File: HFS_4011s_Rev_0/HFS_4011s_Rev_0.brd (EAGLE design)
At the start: 44.5 x 47 mm, 63 parts, among them IC1 CP2104, J1 2X06, J2 2X12, J3 1X02, J4 microUSB, J5 1X02, J6 MOLEX_IGRID_15X2CONNECTOR, Q1 mmbt2222, Q2 mmbt2222, Q3 MMUN2133LT1G, Q4 BSS138, Q5 BSS138, SW2 KMR2, U1 TPS61090RSAR, U2 MCP73831T-2ACI/OT, U3 AD5693R, U4 LM3671MF-3.3/NOPB, X2 ESP32_WROOM32_SKINNY

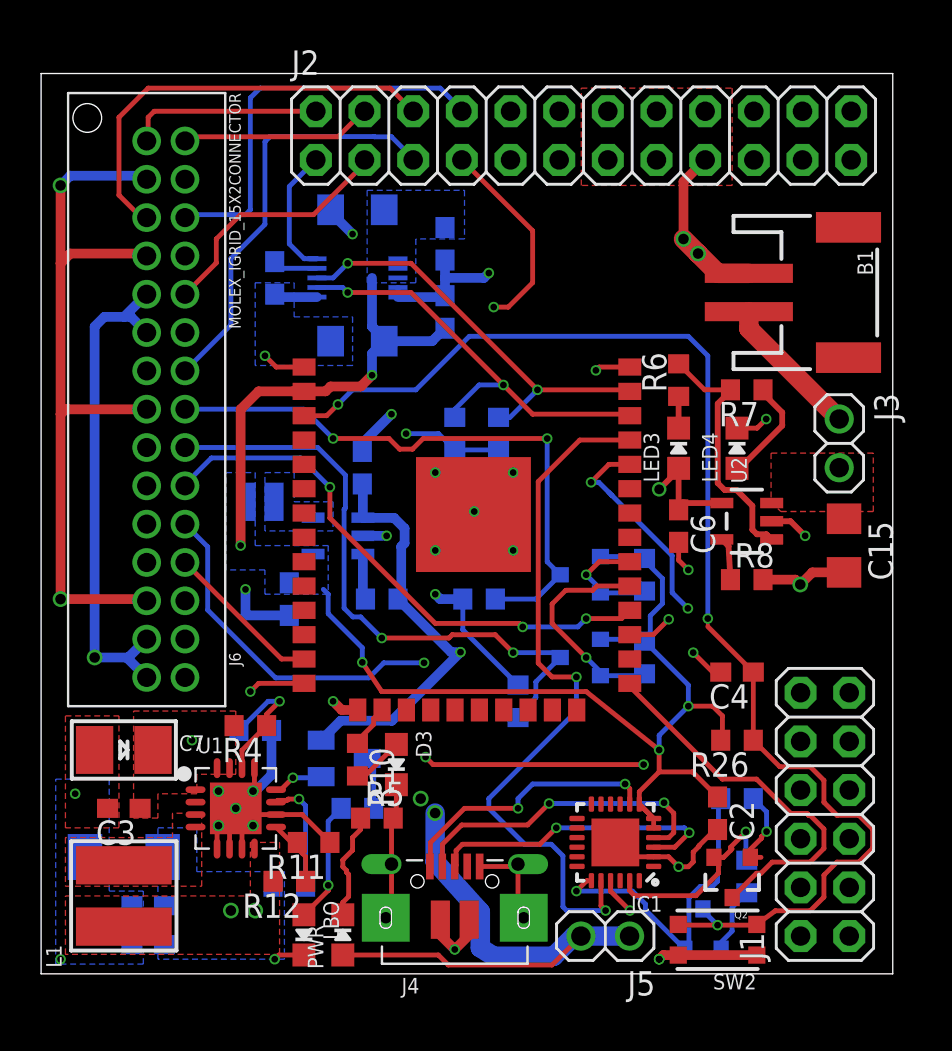
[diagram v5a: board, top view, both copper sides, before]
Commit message: Renumbered components and fixing DRC errors.
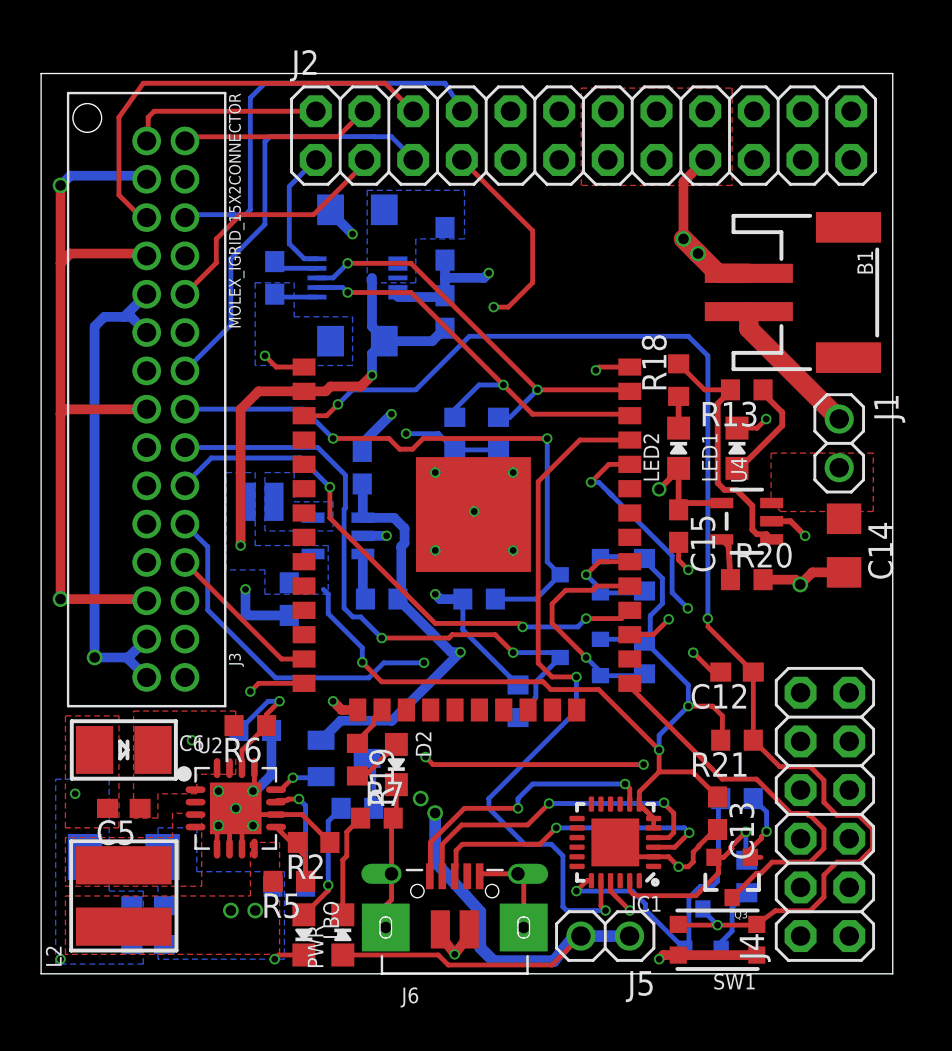
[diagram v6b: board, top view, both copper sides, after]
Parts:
- removed R23: 5.1k, rcl:R0603
- removed R24, R25, R26: 10k, rcl:R0603
- added R1: 100K, rcl:R0603
- added R13, R3: 1K, rcl:R0603
- added R15: 5.1k, rcl:R0603
- C10: value 22uF -> 10uF; device rcl:C0603 -> SparkFun-Retired:EIA3216
- C11: value 10uF -> 0.1uF
- C12: value 10nF -> 1uF
- C13: device SparkFun-Retired:EIA3216 -> rcl:C0603
- C14: value 10uF -> 4.7uF; device SparkFun-Retired:EIA3216 -> rcl:C1206
- C15: value 4.7uF -> 10µF; device rcl:C1206 -> rcl:C0603
- C2: value 10uF -> 22uF
- C3: value 2.2uF -> 10uF
- C4: value 1uF -> 0.1uF
- C5: value 0.1uF -> 2.2uF
- C6: value 10µF -> 100uF/6V; device rcl:C0603 -> microbuilder:EIA3528-21/B-R
- C7: value 100uF/6V -> 10uF; device microbuilder:EIA3528-21/B-R -> SparkFun-Retired:EIA3216
- C9: value 0.1uF -> 10nF
- J1: value 2X06 -> 1X02; device HFS4011sCustom:2X06 -> HFS4011sCustom:1X02
- J3: value 1X02 -> MOLEX_IGRID_15X2CONNECTOR; device HFS4011sCustom:1X02 -> HFS4011sCustom:MOLEX_IGRID15X2CONNECTOR
- J4: value microUSB -> 2X06; device microbuilder:4UCONN_20329 -> HFS4011sCustom:2X06
- J6: value MOLEX_IGRID_15X2CONNECTOR -> microUSB; device HFS4011sCustom:MOLEX_IGRID15X2CONNECTOR -> microbuilder:4UCONN_20329
- L1: value VLC5045-6.8uH -> 2.2uH/NRH2412T2R2MNGH; device microbuilder:INDUCTOR_5X5MM_TDK_VLC5045 -> microbuilder:INDUCTOR_TAIYOYUDEN_NRH2412T
- L2: value 2.2uH/NRH2412T2R2MNGH -> VLC5045-6.8uH; device microbuilder:INDUCTOR_TAIYOYUDEN_NRH2412T -> microbuilder:INDUCTOR_5X5MM_TDK_VLC5045
- Q1: value mmbt2222 -> MMUN2133LT1G; device SparkFun:SOT23-3 -> transistor:SC59-BEC
- Q3: value MMUN2133LT1G -> mmbt2222; device transistor:SC59-BEC -> SparkFun:SOT23-3
- R10: value 1K -> 10k
- R11: value 340K -> 5k
- R12: value 1.87Mohm -> 5k
- R14: value 100K -> 5.1k
- R17: value 5k -> 5.1k
- R18: value 5k -> 470
- R19: value 5.1k -> 1K
- R20: value 1K -> 2k
- R21: value 5.1k -> 10k
- R4: value 1.87Mohm -> 200K
- R5: value 1K -> 1.87Mohm
- R6: value 470 -> 1.87Mohm
- R8: value 2k -> 340K
- R9: value 200K -> 10k
- U1: value TPS61090RSAR -> LM3671MF-3.3/NOPB; device microbuilder:PVQFN-16 -> microbuilder:SOT23-5
- U2: value MCP73831T-2ACI/OT -> TPS61090RSAR; device microbuilder:SOT23-5 -> microbuilder:PVQFN-16
- U4: value LM3671MF-3.3/NOPB -> MCP73831T-2ACI/OT
- moved J3 35.4 mm to (6.35, 30.5)
- moved C4 33.9 mm to (5.59, 1.52), flipped to the bottom, turned to 0 degrees
- moved C12 31.7 mm to (36.3, 15.7), flipped to the top, turned to 180 degrees
- moved C6 31.2 mm to (4.32, 11.7), turned to 0 degrees
- moved C13 31.0 mm to (35.3, 8.38), flipped to the top, turned to 270 degrees
- moved C14 30.9 mm to (41.9, 22.4), flipped to the top, turned to 270 degrees
- moved C7 30.7 mm to (16.5, 39.9), flipped to the bottom, turned to 180 degrees
- moved U2 30.6 mm to (10.2, 8.64), turned to 0 degrees
- moved J6 30.3 mm to (21.6, 4.32), turned to 0 degrees
- moved R7 29.5 mm to (17.5, 8.13), turned to 0 degrees
- moved R8 28.7 mm to (13.0, 4.57), flipped to the bottom, turned to 180 degrees
- moved R6 28.7 mm to (10.9, 13.0), turned to 180 degrees
- moved R9 26.8 mm to (36.8, 5.08), turned to 270 degrees
- moved C1 25.4 mm to (16.8, 26.4), turned to 90 degrees
- moved C2 25.0 mm to (13.0, 19.6), flipped to the bottom
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- renumbered D3 to D2, LED3 to LED2, LED4 to LED1, R22 to R16, SW2 to SW1, X2 to X1
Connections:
- net 3.3V: now also C10.A, C11.1, C13.1, C7.A, J3.P$10, J3.P$12, J3.P$28, J3.P$30, L1.2, R11.2, R12.2, R14.2, R21.2, U1.4; no longer C10.1, C13.A, C14.A, C9.1, J6.P$10, J6.P$12, J6.P$28, J6.P$30, L2.2, R17.2, R18.2, R19.2, R26.2, U4.4
- net 5.0V: now also C5.1, C6.+, J3.P$16, J3.P$26, J3.P$4, J3.P$8, R15.2, R17.2, R6.2, U2.1, U2.15, U2.16; no longer C3.1, C7.+, J6.P$16, J6.P$26, J6.P$4, J6.P$8, R21.2, R23.2, R4.2, U1.1, U1.15, U1.16
- net ANC_SW_H: now also J3.P$23; no longer J6.P$23
- net DTR: now also Q3.2, R9.1; no longer Q2.2, R25.1
- net EN: now also R1.2, U1.3; no longer R14.2, U4.3
- net ENABLE: now also R8.2, U2.11; no longer R2.2, U1.11
- net GND: now also C10.C, C13.2, C14.2, C6.-, C7.C, J3.P$11, J3.P$14, J3.P$18, J3.P$20, J3.P$22, J3.P$24, J3.P$25, J3.P$27, J3.P$29, J3.P$3, J3.P$7, J6.BASE@1, J6.BASE@2, J6.GND, J6.SPRT@1, J6.SPRT@2, J6.SPRT@3, J6.SPRT@4, R2.1, R20.2, R4.1, R7.2, U1.2, U2.10, U2.13, U2.5, U2.6, U2.7, U2.P$18, U2.P$19, U2.P$20, U2.P$21, U2.P$22, U2.THERMAL; no longer C10.2, C13.C, C14.C, C6.2, C7.-, J4.BASE@1, J4.BASE@2, J4.GND, J4.SPRT@1, J4.SPRT@2, J4.SPRT@3, J4.SPRT@4, J6.P$11, J6.P$14, J6.P$18, J6.P$20, J6.P$22, J6.P$24, J6.P$25, J6.P$27, J6.P$29, J6.P$3, J6.P$7, R11.1, R5.2, R8.2, R9.1, U1.10, U1.13, U1.5, U1.6, U1.7, U1.P$18, U1.P$19, U1.P$20, U1.P$21, U1.P$22, U1.THERMAL, U2.2
- net GPIO0: now also Q3.3; no longer Q2.3
- net IO13_A12: now also R19.1; no longer R10.1
- net LBO: now also Q1.B, U2.12; no longer Q3.B, U1.12
- net MIC1_AUD: now also J3.P$9; no longer J6.P$9
- net MIC2_AUD: now also J3.P$13; no longer J6.P$13
- net MOSI_5V: now also J3.P$15, R17.1; no longer J6.P$15, R23.1
- net N$1: now also R18.1; no longer R6.1
- net N$10: now also R7.1; no longer R5.1
- net N$11: now also R4.2, R6.1, U2.14; no longer R4.1, R9.2, U1.14
- net N$12: now also Q2.1, R9.2; no longer Q1.1, R25.2
- net N$13: now also Q3.1, R10.2; no longer Q2.1, R24.2
- net N$14: now also R3.1; no longer R20.1
- net N$15: now also Q1.C, R3.2; no longer Q3.C, R20.2
- net N$16: now also J1.1; no longer J3.1
- net N$17: now also L1.1, U1.5; no longer L2.1, U4.5
- net N$2: now also J6.D+; no longer J4.D+
- net N$20: now also C9.1; no longer C12.1
- net N$3: now also L2.P$2, U2.3, U2.4; no longer L1.P$2, U1.3, U1.4
- net N$4: now also R2.2, R5.1, U2.9; no longer R11.2, R12.1, U1.9
- net N$5: now also R19.2; no longer R10.2
- net N$6: now also J6.D-; no longer J4.D-
- net N$7: now also R13.2, R18.2, U4.1; no longer R6.2, R7.2, U2.1
- net N$8: now also R20.1, U4.5; no longer R8.1, U2.5
- net N$9: now also R13.1; no longer R7.1
- net PB1_H: now also J3.P$21; no longer J6.P$21
- net PB2_H: now also J3.P$19; no longer J6.P$19
- net RESET: now also C12.1, Q2.3, R21.1; no longer C4.1, Q1.3, R26.1
- net RTS: now also Q2.2, R10.1; no longer Q1.2, R24.1
- net SCK: now also R14.1; no longer R19.1
- net SCK_5V: now also J3.P$17, R15.1; no longer J6.P$17, R21.1
- net SCL: now also R12.1; no longer R17.1
- net SDA: now also R11.1; no longer R18.1
- net SPKR_L_N: now also J3.P$1; no longer J6.P$1
- net SPKR_L_P: now also J3.P$2; no longer J6.P$2
- net SPKR_R_N: now also J3.P$5; no longer J6.P$5
- net SPKR_R_P: now also J3.P$6; no longer J6.P$6
- net VBAT: now also C14.1, C3.1, C4.1, J1.2, L2.P$1, Q1.E, R1.1, R5.2, R8.1, U1.1, U2.8, U4.3; no longer C11.1, C15.1, C5.1, J3.2, L1.P$1, Q3.E, R12.2, R14.1, R2.1, U1.8, U2.3, U4.1
- net VBUS: now also C15.1, J6.VBUS, U4.4; no longer C6.1, J4.VBUS, U2.4
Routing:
- net GND: track 109.7 -> 97.8 mm, vias 27 -> 26
- net 3.3V: track 139.5 -> 138.6 mm
- net N$6: track 16.6 -> 17.1 mm

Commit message: Finished adding all silkscreen text. Got rid of some clearance errors. Seems like everything is set for fab.
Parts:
- J3: value MOLEX_IGRID_15X2CONNECTOR -> (none)
- moved LBO 0.25 mm to (13.5, 2.03)
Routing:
- net GND: track 97.8 -> 100.0 mm
